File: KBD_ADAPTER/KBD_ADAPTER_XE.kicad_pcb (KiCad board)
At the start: 2 copper layers, 62 x 16.5 mm, 2 parts, among them J1 Conn_01x24, J2 Conn_02x17_Counter_Clockwise

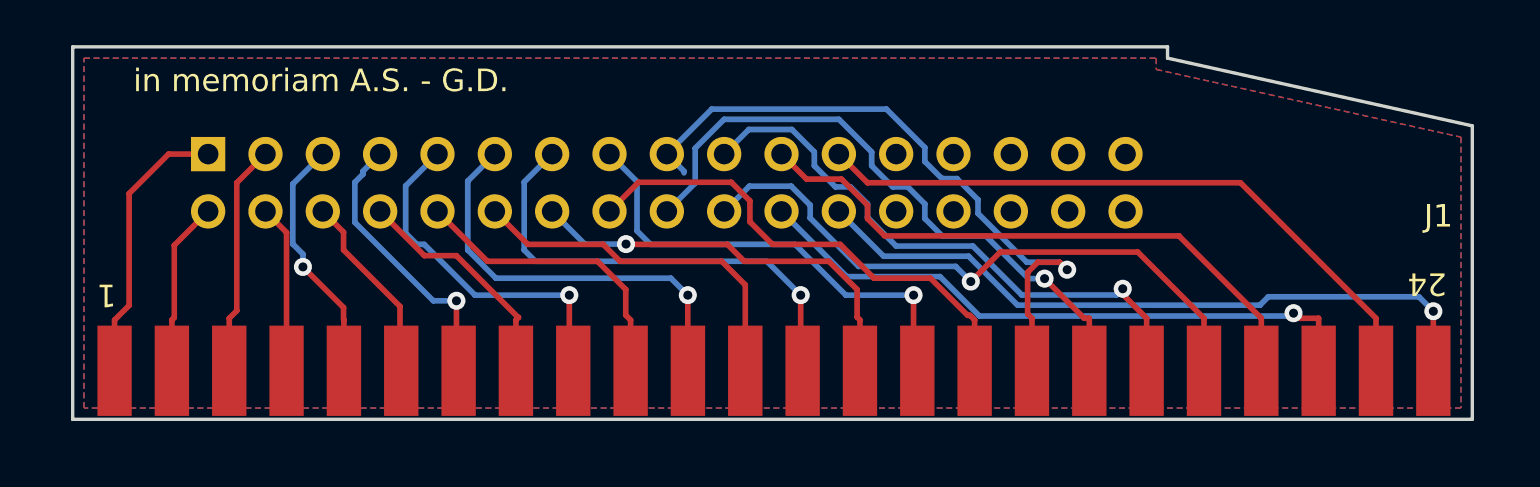
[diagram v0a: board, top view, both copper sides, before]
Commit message: New FPC cable. No Flat Ribbon. It was too big!
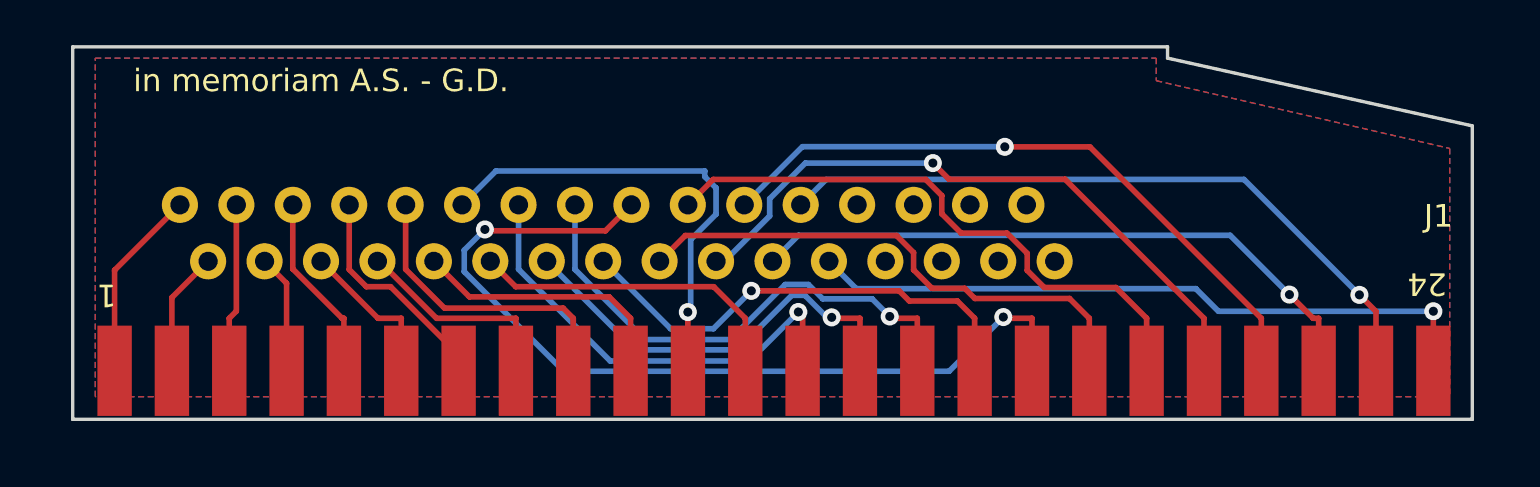
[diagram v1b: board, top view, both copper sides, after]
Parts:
- J2: value Conn_02x17_Counter_Clockwise -> Conn_01x32; footprint RetroBitLab:IDC-Header_2x17_P2.54mm_Vertical_Lock -> RetroBitLab:FFC-1.25mm-RA-5204403245
- moved J2 19.1 mm to (137.8, 103.8), turned to 0 degrees
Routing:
- net IN_0: track 29.9 -> 39.6 mm, vias 1 -> 2
- net OUT_0: track 28.0 -> 23.8 mm, vias 1 -> 0
- net VCC: track 12.3 -> 8.55 mm
- net GND: track 10.3 -> 7.48 mm
- net OUT_3: track 11.1 -> 8.34 mm, vias 1 -> 0
- net OUT_7: track 12.6 -> 9.98 mm, vias 1 -> 0
- net OUT_2: track 20.8 -> 23.3 mm
- net START: track 26.9 -> 29.4 mm, vias 0 -> 1
- net IN_7: track 15.9 -> 13.5 mm, vias 1 -> 0
- net IN_1: track 18.7 -> 20.9 mm
- net J_LED: track 7.72 -> 5.51 mm
- net IN_6: track 7.45 -> 5.25 mm
- net OPTION: track 29.1 -> 31.0 mm, vias 0 -> 1
- net OUT_6: track 16.2 -> 14.7 mm
- net OUT_5: track 8.50 -> 6.93 mm
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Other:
- rule pad_to_mask_clearance: 0.051 -> 0

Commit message: The height of the board is very tight with the PCB installed. It needs to be at maximum of 12.3mm, so use a vertical (so become angled) connector. The original connector can be used but with a keyboard installed in the top case (new case)
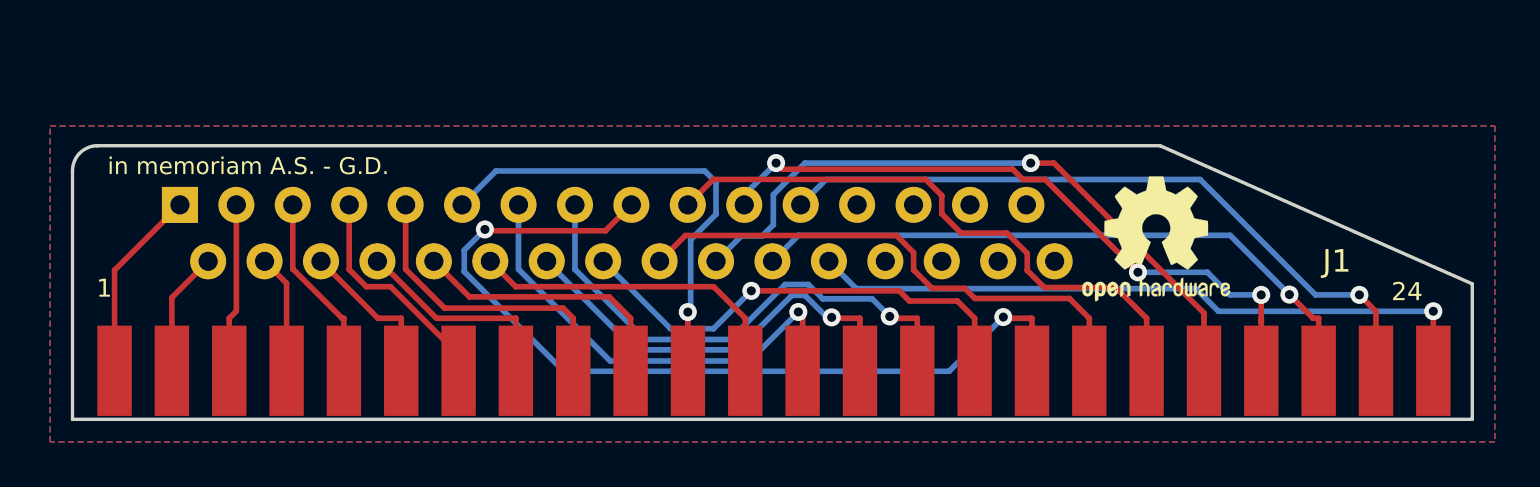
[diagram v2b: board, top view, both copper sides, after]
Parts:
- added REF**: OSHW-Logo2_7.3x6mm_SilkScreen, Symbol:OSHW-Logo2_7.3x6mm_SilkScreen, F.Cu at (161.0, 104.0)
- J2: footprint RetroBitLab:FFC-1.25mm-RA-5204403245 -> RetroBitLab:MOLEX-FFC-1.25mm-RA-52045-3245
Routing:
- net RSC: track 29.0 -> 29.9 mm
- net START: track 29.4 -> 29.9 mm, vias 1 -> 3
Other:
- board size 62 x 16.5 mm -> 62 x 12.1 mm
- board text added: "ATARI XE keyboard adapter by RetroBitLab Tech Guy"
- board text added: "PCB Thickness 0.6mm"
- board text removed: "ATARI XL/XE keyboard adapter by RetroBitLab Tech Guy"
